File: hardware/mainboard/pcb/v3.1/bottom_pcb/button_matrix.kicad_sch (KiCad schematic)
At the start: 37 parts, among them U11 touch_but_square, U12 touch_but_square, U13 touch_but_square, U14 touch_but_square, U15 touch_but_square, U16 touch_but_square, U17 touch_but_square, U18 touch_but_square, U19 74hc4066, U20 74hc4066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

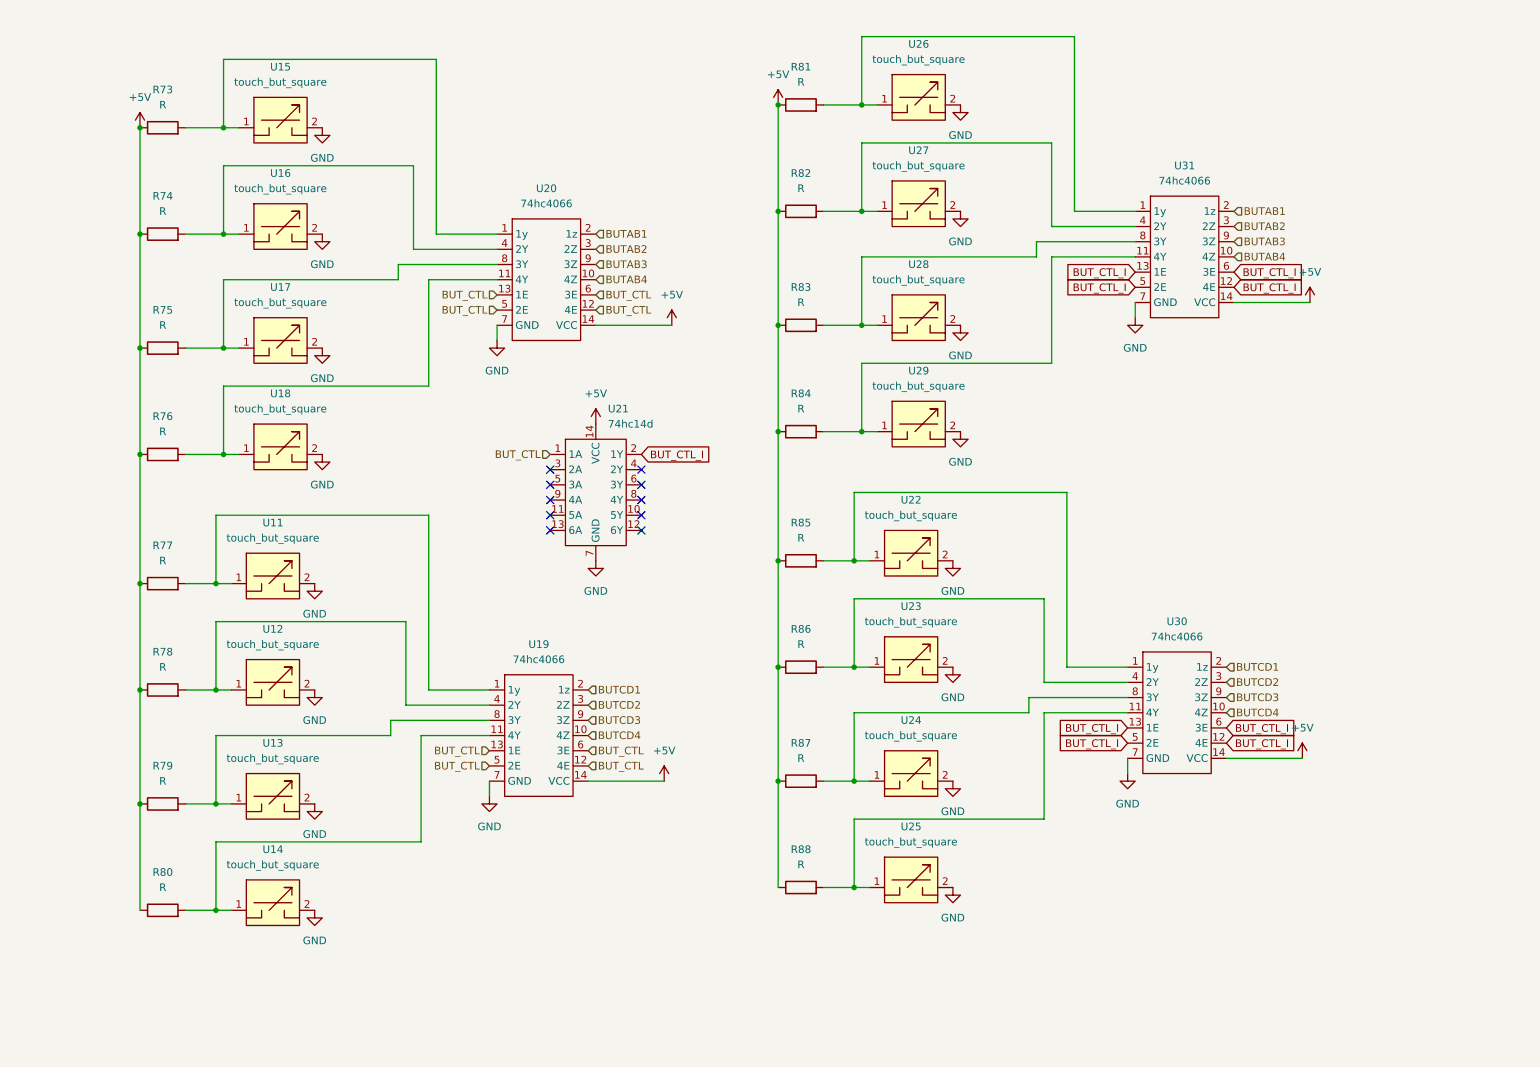
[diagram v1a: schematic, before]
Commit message: update to 74hc4053aft
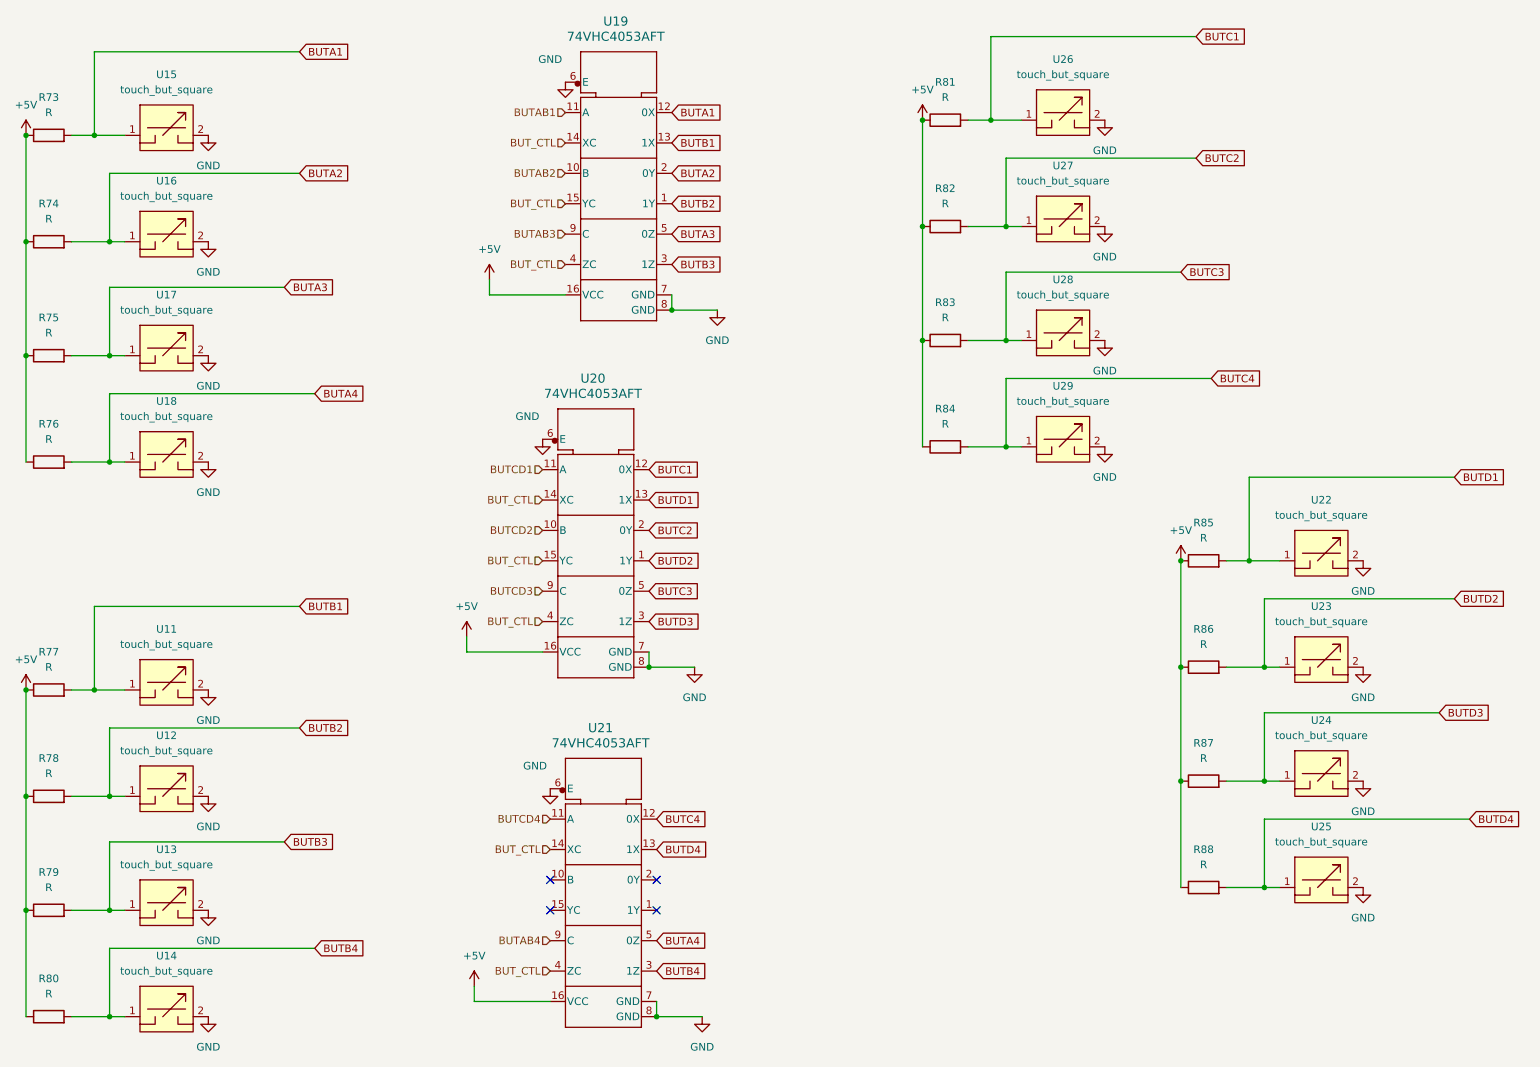
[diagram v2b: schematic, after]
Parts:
- removed U19, U20, U30, U31: 74hc4066, Package_SO:SOIC-14_3.9x8.7mm_P1.27mm, symbol 3dAudioSym:74hc4066
- removed U21: 74hc14d, Package_SO:SOIC-14_3.9x8.7mm_P1.27mm, symbol 3dAudioSym:74hc14d
- added U19, U20, U21: 74VHC4053AFT, 3dAudioFoot:74vhc4053aft, symbol 3dAudioSym:74VHC4053AFT
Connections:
- net +5V: now also U19.16 (VCC), U20.16 (VCC), U21.16 (VCC)
- net BUTAB1: now also U19.11 (A)
- net BUTAB2: now also U19.10 (B)
- net BUTAB3: now also U19.9 (C)
- net BUTAB4: now also U21.9 (C)
- net BUTCD1: now also U20.11 (A)
- net BUTCD2: now also U20.10 (B)
- net BUTCD3: now also U20.9 (C)
- net BUTCD4: now also U21.11 (A)
- net BUT_CTL: now also U19.14 (XC), U19.15 (YC), U19.4 (ZC), U20.14 (XC), U20.15 (YC), U20.4 (ZC), U21.14 (XC), U21.4 (ZC)
- net GND: now also U19.6 (E), U19.7 (GND), U19.8 (GND), U20.6 (E), U20.7 (GND), U20.8 (GND), U21.6 (E), U21.7 (GND), U21.8 (GND)
- net BUTD4: now reaches R88.2, U25.1
- net BUTD4: now also U21.13 (1X)
- net BUTB2: now reaches R78.2, U12.1
- net BUTB2: now also U19.1 (1Y)
- net BUTC4: now reaches R84.2, U29.1
- net BUTC4: now also U21.12 (0X)
- net BUTD2: now reaches R86.2, U23.1
- net BUTD2: now also U20.1 (1Y)
- net BUTB4: now reaches R80.2, U14.1
- net BUTB4: now also U21.3 (1Z)
- net BUTB3: now reaches R79.2, U13.1
- net BUTB3: now also U19.3 (1Z)
- net BUTA1: now reaches R73.2, U15.1
- net BUTA1: now also U19.12 (0X)
- net BUTD3: now reaches R87.2, U24.1
- net BUTD3: now also U20.3 (1Z)
- net BUTC3: now reaches R83.2, U28.1
- net BUTC3: now also U20.5 (0Z)
- net BUTA4: now reaches R76.2, U18.1
- net BUTA4: now also U21.5 (0Z)
- net BUTD1: now reaches R85.2, U22.1
- net BUTD1: now also U20.13 (1X)
- net BUTA3: now reaches R75.2, U17.1
- net BUTA3: now also U19.5 (0Z)
- net BUTA2: now reaches R74.2, U16.1
- net BUTA2: now also U19.2 (0Y)
- net BUTC2: now reaches R82.2, U27.1
- net BUTC2: now also U20.2 (0Y)
- net BUTC1: now reaches R81.2, U26.1
- net BUTC1: now also U20.12 (0X)
- net BUTB1: now reaches R77.2, U11.1
- net BUTB1: now also U19.13 (1X)
- no-connect marks 10 -> 4
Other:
- moved on the sheet: R73, R74, R75, R76, U11, U12, U13, U14, U15, U16, U17, U18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
